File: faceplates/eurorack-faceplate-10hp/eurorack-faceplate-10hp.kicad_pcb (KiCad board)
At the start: 2 copper layers, 50.5 x 133.3 mm, 4 parts

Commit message: Moving mounting holes
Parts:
- moved REF** 2.42 mm to (5.08, 130.3)
- moved REF** 2.42 mm to (5.08, 3.00)
- moved REF** 2.36 mm to (45.4, 130.3)
- moved REF** 2.36 mm to (45.4, 3.00)
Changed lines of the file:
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@@
   (net 0 "")
   (footprint "MountingHole:MountingHole_3.2mm_M3" (layer "F.Cu")
-    (at 7.5 130.35)
+    (at 5.08 130.35)
     (descr "Mounting Hole 3.2mm, no annular, M3")
     (tags "mounting hole 3.2mm no annular m3")
@@
   )
   (footprint "MountingHole:MountingHole_3.2mm_M3" (layer "F.Cu")
-    (at 43.06 130.35)
+    (at 45.42 130.35)
     (descr "Mounting Hole 3.2mm, no annular, M3")
     (tags "mounting hole 3.2mm no annular m3")
@@
   )
   (footprint "MountingHole:MountingHole_3.2mm_M3" (layer "F.Cu")
-    (at 43.06 3)
+    (at 45.42 3)
     (descr "Mounting Hole 3.2mm, no annular, M3")
     (tags "mounting hole 3.2mm no annular m3")
@@
   )
   (footprint "MountingHole:MountingHole_3.2mm_M3" (layer "F.Cu")
-    (at 7.5 3)
+    (at 5.08 3)
     (descr "Mounting Hole 3.2mm, no annular, M3")
     (tags "mounting hole 3.2mm no annular m3")
@@
   (gr_line (start 0 0) (end 50.5 0) (layer "Edge.Cuts") (width 0.1))
   (gr_line (start 50.5 133.35) (end 0 133.35) (layer "Edge.Cuts") (width 0.1))
+  (dimension (type aligned) (layer "User.1")
+    (pts (xy 5.08 3) (xy 0 3))
+    (height 9)
+    (gr_text "5.0800 mm" (at 2.54 -7.15) (layer "User.1")
+      (effects (font (size 1 1) (thickness 0.15)))
+    )
+    (format (units 3) (units_format 1) (precision 4))
+    (style (thickness 0.1) (arrow_length 1.27) (text_position_mode 0) (extension_height 0.58642) (extension_offset 0.5) keep_text_aligned)
+  )
 )

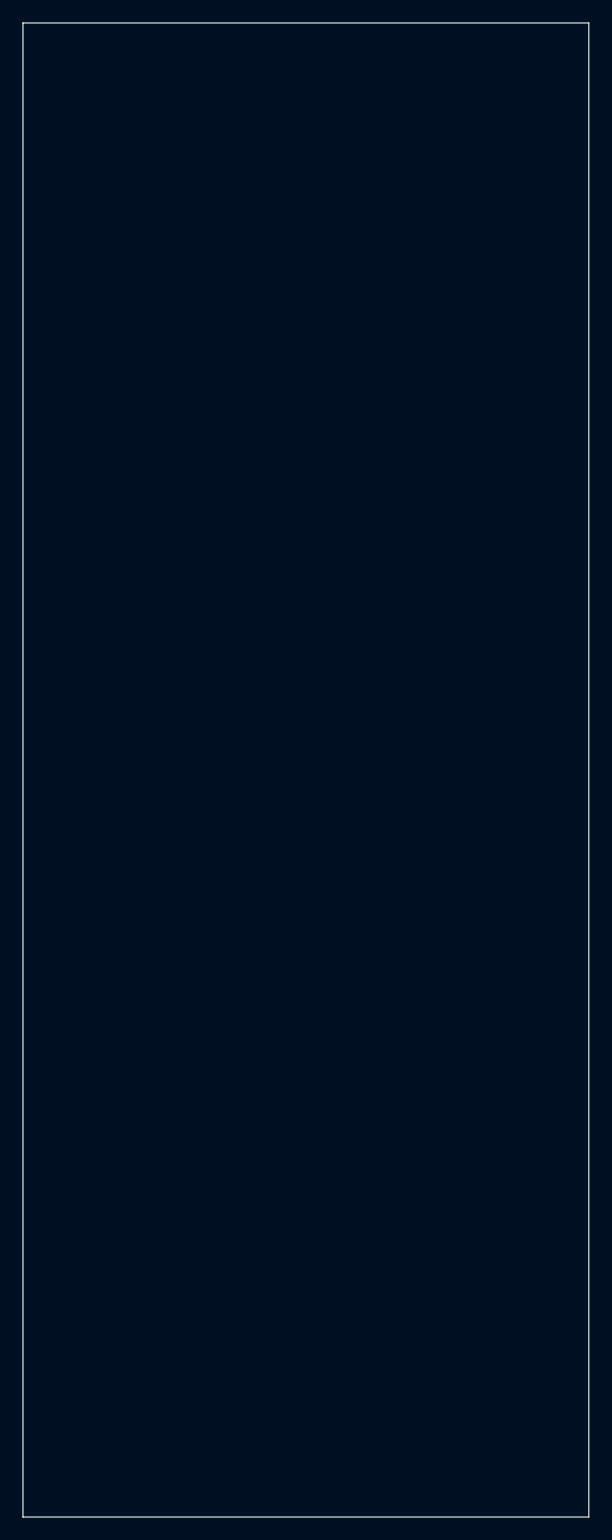
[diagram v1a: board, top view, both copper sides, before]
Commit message: Correcting panel height
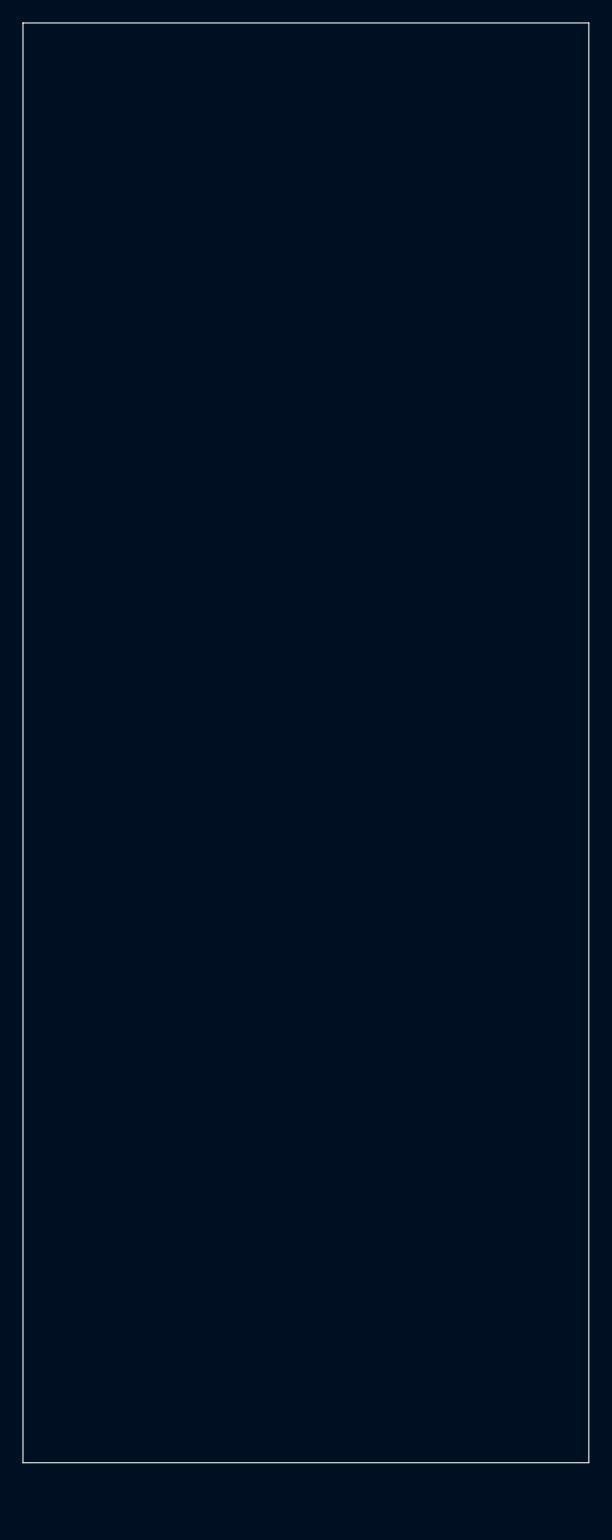
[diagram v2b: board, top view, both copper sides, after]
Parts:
- moved REF** 4.85 mm to (5.08, 125.5)
- moved REF** 4.85 mm to (45.4, 125.5)
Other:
- board size 50.5 x 133.3 mm -> 50.5 x 128.5 mm
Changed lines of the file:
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@@
   (net 0 "")
   (footprint "MountingHole:MountingHole_3.2mm_M3" (layer "F.Cu")
-    (at 5.08 130.35)
+    (at 5.08 125.5)
     (descr "Mounting Hole 3.2mm, no annular, M3")
     (tags "mounting hole 3.2mm no annular m3")
@@
   )
   (footprint "MountingHole:MountingHole_3.2mm_M3" (layer "F.Cu")
-    (at 45.42 130.35)
+    (at 45.42 125.5)
     (descr "Mounting Hole 3.2mm, no annular, M3")
     (tags "mounting hole 3.2mm no annular m3")
@@
     (pad "" np_thru_hole oval locked (at 0 0) (size 7 3.2) (drill oval 7 3.2) (layers F&B.Cu *.Mask))
   )
-  (gr_line (start 50.5 0) (end 50.5 133.35) (layer "Edge.Cuts") (width 0.1))
-  (gr_line (start 0 133.35) (end 0 0) (layer "Edge.Cuts") (width 0.1))
+  (gr_line (start 50.5 0) (end 50.5 128.5) (layer "Edge.Cuts") (width 0.1))
+  (gr_line (start 0 128.5) (end 0 0) (layer "Edge.Cuts") (width 0.1))
   (gr_line (start 0 0) (end 50.5 0) (layer "Edge.Cuts") (width 0.1))
-  (gr_line (start 50.5 133.35) (end 0 133.35) (layer "Edge.Cuts") (width 0.1))
+  (gr_line (start 50.5 128.5) (end 0 128.5) (layer "Edge.Cuts") (width 0.1))
   (dimension (type aligned) (layer "User.1")
     (pts (xy 5.08 3) (xy 0 3))
